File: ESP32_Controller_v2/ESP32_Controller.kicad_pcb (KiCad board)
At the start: 2 copper layers, 85.1 x 89.9 mm, 34 parts, among them J1 Conn_01x03, J10 Conn_01x02, J2 Conn_01x03, J3 Conn_01x03, J4 Conn_01x03, J5 Conn_01x03, J6 Conn_01x03, J7 Conn_01x03, J8 Conn_01x03, J9 Conn_01x02, U1 ESP32-DEVKITC, U2 LM7805_TO220, U3 SN74HCT245N

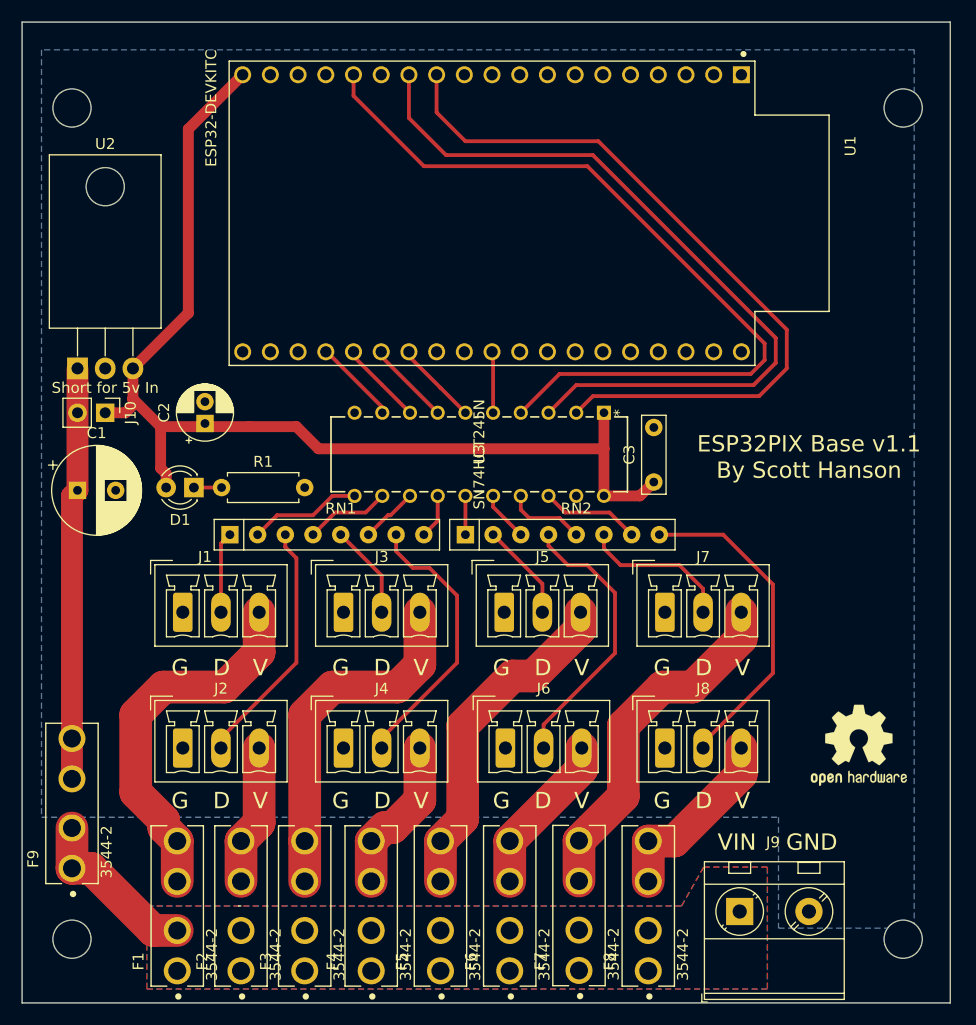
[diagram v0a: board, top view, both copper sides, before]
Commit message: add plug in 3 to 4 adapter
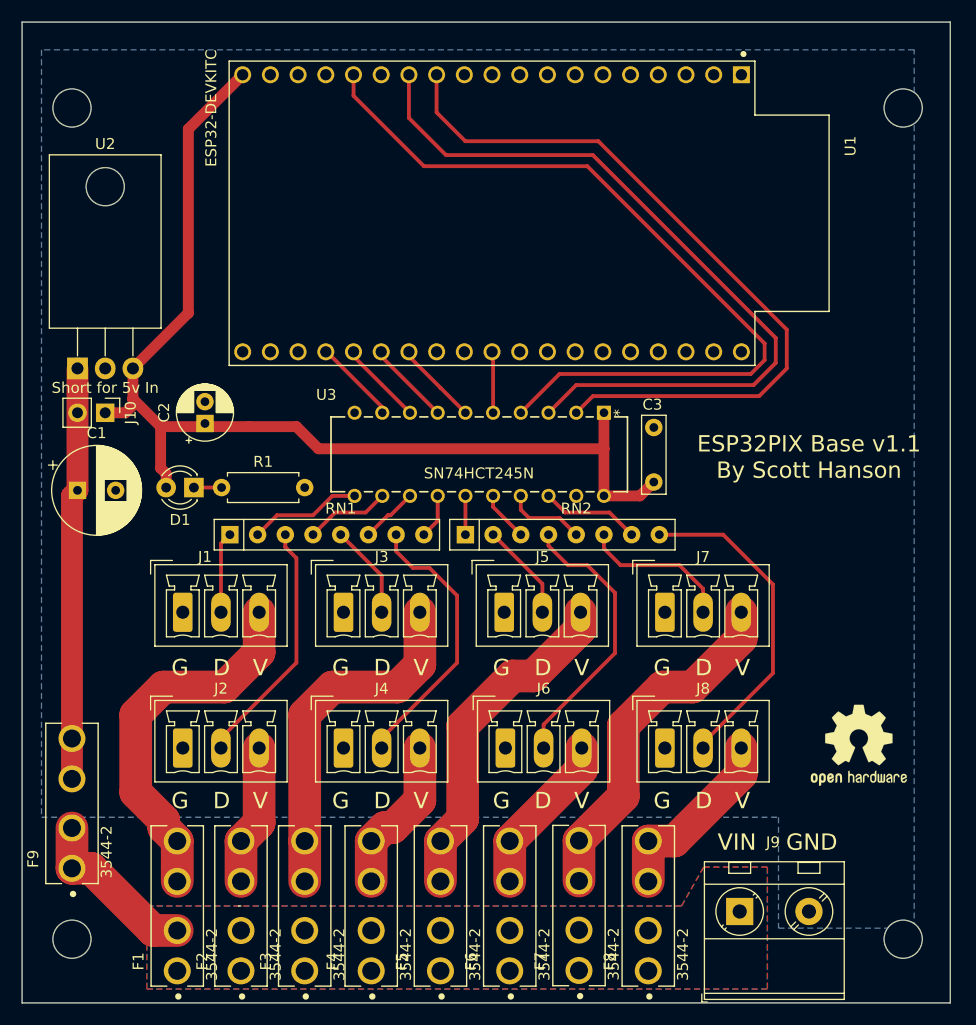
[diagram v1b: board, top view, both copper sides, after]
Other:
- net class 5v removed
- net class Default removed
- net class Power removed
- net class Vin removed
